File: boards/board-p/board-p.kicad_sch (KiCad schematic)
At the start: 0 parts

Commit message: feat: capture Board P schematic from the locked net table
Generated by scripts/schgen/gen_board_p.py: all 24 components placed
with global labels per pin, verified two ways with kicad-cli --
ERC passes with zero violations (including warnings) and the exported
netlist matches doc/architecture/board-p.mdx net-for-net (17 nets,
89 nodes, 6 intentional no-connects).

- symbols lib: all pins retyped passive (EasyEDA import had bogus
  Input types), Conn_1x04/Conn_1x08 pogo-pad symbols added
- footprints: PogoPad_1x04/1x08_P2.54mm hand-made pad arrays added
- C2/C35 use C14663 (0603, Basic) per the recommended Extended-fee
  swap in the docs; DNP parts (R17/R18, D6/D7) carry the dnp flag
- verify_netlist.py re-checks the schematic against the net table

Co-Authored-By: Claude <noreply@anthropic.com>
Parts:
- added C1: 10uF/50V, zudo-led-lamp:C1206, symbol zudo-led-lamp:CL31A106KBHNNNE
- added C2, C35: 100nF/50V, zudo-led-lamp:C0603, symbol zudo-led-lamp:CC0603KRX7R9BB104
- added C30, C34: 1uF/50V, zudo-led-lamp:C0603, symbol zudo-led-lamp:CL10A105KB8NNNC
- added D5: SMAJ20A, zudo-led-lamp:SMA_L4.2-W2.6-LS5.3-RD, symbol zudo-led-lamp:SMAJ20A_C571370
- added D6, D7: PESD24VS1UB, zudo-led-lamp:SOD-523_L1.2-W0.8-LS1.6-RD, symbol zudo-led-lamp:PESD24VS1UB,115
- added J1: TYPE-C-31-M-17, zudo-led-lamp:USB-C-SMD_10P-P1.00-L6.8-W8.9, symbol zudo-led-lamp:TYPE-C-31-M-17
- added J2: PogoPad_1x4_NVM_I2C, zudo-led-lamp:PogoPad_1x04_P2.54mm, symbol zudo-led-lamp:Conn_1x04
- added J3: PogoPad_1x8_Debug, zudo-led-lamp:PogoPad_1x08_P2.54mm, symbol zudo-led-lamp:Conn_1x08
- added JOUT1: B6B-XH-A(LF)(SN), zudo-led-lamp:CONN-TH_6P-P2.50_B6B-XH-A-LF-SN, symbol zudo-led-lamp:B6B-XH-A
- added Q1: AO3401A, zudo-led-lamp:SOT-23_L2.9-W1.3-P1.90-LS2.4-BR, symbol zudo-led-lamp:AO3401A_C347476
- added R11: 100k, zudo-led-lamp:R0603, symbol zudo-led-lamp:0603WAF1003T5E
- added R12: 56k, zudo-led-lamp:R0603, symbol zudo-led-lamp:0603WAF5602T5E
- added R13, R14: 470R, zudo-led-lamp:R0603, symbol zudo-led-lamp:0603WAF4700T5E
- added R15, R16: 4.7k, zudo-led-lamp:R0603, symbol zudo-led-lamp:0603WAF4701T5E
- added R17, R18: 5.1k, zudo-led-lamp:R0603, symbol zudo-led-lamp:0603WAF5101T5E
- added R19, R20: 0R, zudo-led-lamp:R0603, symbol zudo-led-lamp:0603WAF0000T5E
- added U1: STUSB4500QTR, zudo-led-lamp:QFN-24_L4.0-W4.0-P0.50-BL-EP2.8, symbol zudo-led-lamp:STUSB4500QTR
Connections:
- new net ATT: J3.6, JOUT1.3, U1.11 (ATTACH)
- new net CC1: D6.1 (C), J1.3 (A5), R17.1, R19.2, U1.2 (CC1)
- new net CC1DB: J3.1, R19.1, U1.1 (CC1DB)
- new net CC2: D7.1 (C), J1.4 (B5), R18.1, R20.2, U1.4 (CC2)
- new net CC2DB: J3.2, R20.1, U1.5 (CC2DB)
- new net DISCH: R13.2, U1.9 (DISCH)
- new net GND: C1.1, C2.1, C30.1, C34.2, C35.2, D5.2 (A), D6.2 (A), D7.2 (A), J1.0, J1.1 (B12), J1.6 (A12), J2.3, J3.5, JOUT1.5, JOUT1.6, R17.2, R18.2, U1.10 (GND), U1.12 (ADDR0), U1.13 (ADDR1), U1.22 (VSYS), U1.25 (EP), U1.6 (RESET)
- new net PDOK: J3.7, JOUT1.4, U1.20 (POWER_OK2)
- new net Q1_G: C35.1, Q1.1 (G), R11.1, R12.2
- new net SCL: J2.1, R15.1, U1.7 (SCL)
- new net SDA: J2.2, R16.1, U1.8 (SDA)
- new net VBEN: J3.8, R12.1, U1.16 (VBUS_EN_SNK)
- new net VBUS_IN: C1.2, C2.2, D5.1 (C), J1.2 (B9), J1.5 (A9), J3.4, Q1.2 (S), R11.2, R14.1, U1.24 (VDD)
- new net VBUS_OUT: JOUT1.1, JOUT1.2, Q1.3 (D), R13.1
- new net VBUS_VS_DISCH: R14.2, U1.18 (VBUS_VS_DISCH)
- new net VREG_1V2: C34.1, U1.21 (VREG_1V2)
- new net VREG_2V7: C30.2, J3.3, R15.2, R16.2, U1.23 (VREG_2V7)
- no-connect marks 0 -> 6

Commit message: feat: capture Board L schematic; refactor generator into spec-driven core
Board L: all 68 components (driver, LED array 8x3, logic rail, MCU,
encoder, debug pads) captured from the locked net table in
doc/architecture/board-l.mdx. ERC passes with zero violations and the
exported netlist matches the spec: 45 nets, 178 nodes, 11 intentional
no-connects. Board P regenerated through the same pipeline, still
ERC-clean and netlist-verified.

- scripts/schgen split into schgen_core.py + board_p_spec.py /
  board_l_spec.py + generic gen_schematic.py / verify_netlist.py,
  so the net table lives in exactly one place per board
- symbols lib normalized via kicad-cli sym upgrade (two inductor
  symbols were in legacy KiCad 6 format and tripped
  lib_symbol_mismatch ERC warnings); Conn_1x03 symbol added
- PogoPad_1x03_P2.54mm hand-made UART pad footprint added
- J3 (SWD header) and J4 (UART pads) carry the DNP flag: footprint
  only, excluded from the assembly BOM per the bring-up plan
- LED polarity taken from the symbol drawing: pin 1 = cathode,
  pin 2 = anode; EC11 push-button terminals D/E left no-connect

Co-Authored-By: Claude <noreply@anthropic.com>
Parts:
- D6, D7, R17, R18: DNP DNP -> (none)
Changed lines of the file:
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@@
 			)
+		)
+		(pin "0"
+		)
+		(pin "0"
+		)
+		(pin "0"
+		)
+		(pin "0"
 		)
 		(pin "1"
@@
 		(pin "6"
 		)
-		(pin "0"
-		)
-		(pin "0"
-		)
-		(pin "0"
-		)
-		(pin "0"
-		)
-		(instances
-			(project "board-p"
-				(path "/b2dc3f53-49f5-4fb9-8f78-98d4bdbdbabb"
+		(instances
+			(project "board-p"
+				(path "/2f50887c-fd80-4f71-a2f8-d8c1a887c3bf"
 					(reference "J1")
 					(unit 1)
@@
 		(instances
 			(project "board-p"
-				(path "/b2dc3f53-49f5-4fb9-8f78-98d4bdbdbabb"
+				(path "/2f50887c-fd80-4f71-a2f8-d8c1a887c3bf"
 					(reference "U1")
 					(unit 1)
@@
 			)
 		)
+		(pin "1"
+		)
+		(pin "2"
+		)
 		(pin "3"
 		)
-		(pin "1"
-		)
-		(pin "2"
-		)
-		(instances
-			(project "board-p"
-				(path "/b2dc3f53-49f5-4fb9-8f78-98d4bdbdbabb"
+		(instances
+			(project "board-p"
+				(path "/2f50887c-fd80-4f71-a2f8-d8c1a887c3bf"
 					(reference "Q1")
 					(unit 1)
@@
 			)
 		)
-		(pin "2"
-		)
-		(pin "1"
-		)
-		(instances
-			(project "board-p"
-				(path "/b2dc3f53-49f5-4fb9-8f78-98d4bdbdbabb"
+		(pin "1"
+		)
+		(pin "2"
+		)
+		(instances
+			(project "board-p"
+				(path "/2f50887c-fd80-4f71-a2f8-d8c1a887c3bf"
 					(reference "D5")
 					(unit 1)
@@
 			)
 		)
-		(property "DNP" "DNP"
-			(at 228.6 175.26 0)
-			(effects
-				(font (size 1.27 1.27))
-				(hide yes)
-			)
-		)
-		(pin "2"
-		)
-		(pin "1"
-		)
-		(instances
-			(project "board-p"
-				(path "/b2dc3f53-49f5-4fb9-8f78-98d4bdbdbabb"
+		(pin "1"
+		)
+		(pin "2"
+		)
+		(instances
+			(project "board-p"
+				(path "/2f50887c-fd80-4f71-a2f8-d8c1a887c3bf"
 					(reference "D6")
 					(unit 1)
@@
 			)
 		)
-		(property "DNP" "DNP"
-			(at 190.5 226.06 0)
-			(effects
-				(font (size 1.27 1.27))
-				(hide yes)
-			)
-		)
-		(pin "2"
-		)
-		(pin "1"
-		)
-		(instances
-			(project "board-p"
-				(path "/b2dc3f53-49f5-4fb9-8f78-98d4bdbdbabb"
+		(pin "1"
+		)
+		(pin "2"
+		)
+		(instances
+			(project "board-p"
+				(path "/2f50887c-fd80-4f71-a2f8-d8c1a887c3bf"
 					(reference "D7")
 					(unit 1)
@@
 		(instances
 			(project "board-p"
-				(path "/b2dc3f53-49f5-4fb9-8f78-98d4bdbdbabb"
+				(path "/2f50887c-fd80-4f71-a2f8-d8c1a887c3bf"
 					(reference "C1")
 					(unit 1)
@@
 		(instances
 			(project "board-p"
-				(path "/b2dc3f53-49f5-4fb9-8f78-98d4bdbdbabb"
+				(path "/2f50887c-fd80-4f71-a2f8-d8c1a887c3bf"
 					(reference "C2")
 					(unit 1)
@@
 			)
 		)
-		(pin "2"
-		)
-		(pin "1"
-		)
-		(instances
-			(project "board-p"
-				(path "/b2dc3f53-49f5-4fb9-8f78-98d4bdbdbabb"
+		(pin "1"
+		)
+		(pin "2"
+		)
+		(instances
+			(project "board-p"
+				(path "/2f50887c-fd80-4f71-a2f8-d8c1a887c3bf"
 					(reference "C30")
 					(unit 1)
@@
 			)
 		)
-		(pin "2"
-		)
-		(pin "1"
-		)
-		(instances
-			(project "board-p"
-				(path "/b2dc3f53-49f5-4fb9-8f78-98d4bdbdbabb"
+		(pin "1"
+		)
+		(pin "2"
+		)
+		(instances
+			(project "board-p"
+				(path "/2f50887c-fd80-4f71-a2f8-d8c1a887c3bf"
 					(reference "C34")
 					(unit 1)
@@
 		(instances
 			(project "board-p"
-				(path "/b2dc3f53-49f5-4fb9-8f78-98d4bdbdbabb"
+				(path "/2f50887c-fd80-4f71-a2f8-d8c1a887c3bf"
 					(reference "C35")
 					(unit 1)
@@
 			)
 		)
-		(pin "2"
-		)
-		(pin "1"
-		)
-		(instances
-			(project "board-p"
-				(path "/b2dc3f53-49f5-4fb9-8f78-98d4bdbdbabb"
+		(pin "1"
+		)
+		(pin "2"
+		)
+		(instances
+			(project "board-p"
+				(path "/2f50887c-fd80-4f71-a2f8-d8c1a887c3bf"
 					(reference "R11")
 					(unit 1)
@@
 			)
 		)
-		(pin "2"
-		)
-		(pin "1"
-		)
-		(instances
-			(project "board-p"
-				(path "/b2dc3f53-49f5-4fb9-8f78-98d4bdbdbabb"
+		(pin "1"
+		)
+		(pin "2"
+		)
+		(instances
+			(project "board-p"
+				(path "/2f50887c-fd80-4f71-a2f8-d8c1a887c3bf"
 					(reference "R12")
 					(unit 1)
@@
 			)
 		)
-		(pin "2"
-		)
-		(pin "1"
-		)
-		(instances
-			(project "board-p"
-				(path "/b2dc3f53-49f5-4fb9-8f78-98d4bdbdbabb"
+		(pin "1"
+		)
+		(pin "2"
+		)
+		(instances
+			(project "board-p"
+				(path "/2f50887c-fd80-4f71-a2f8-d8c1a887c3bf"
 					(reference "R13")
 					(unit 1)
@@
 			)
 		)
-		(pin "2"
-		)
-		(pin "1"
-		)
-		(instances
-			(project "board-p"
-				(path "/b2dc3f53-49f5-4fb9-8f78-98d4bdbdbabb"
+		(pin "1"
+		)
+		(pin "2"
+		)
+		(instances
+			(project "board-p"
+				(path "/2f50887c-fd80-4f71-a2f8-d8c1a887c3bf"
 					(reference "R14")
 					(unit 1)
@@
 			)
 		)
-		(pin "2"
-		)
-		(pin "1"
-		)
-		(instances
-			(project "board-p"
-				(path "/b2dc3f53-49f5-4fb9-8f78-98d4bdbdbabb"
+		(pin "1"
+		)
+		(pin "2"
+		)
+		(instances
+			(project "board-p"
+				(path "/2f50887c-fd80-4f71-a2f8-d8c1a887c3bf"
 					(reference "R15")
 					(unit 1)
@@
 			)
 		)
-		(pin "2"
-		)
-		(pin "1"
-		)
-		(instances
-			(project "board-p"
-				(path "/b2dc3f53-49f5-4fb9-8f78-98d4bdbdbabb"
+		(pin "1"
+		)
+		(pin "2"
+		)
+		(instances
+			(project "board-p"
+				(path "/2f50887c-fd80-4f71-a2f8-d8c1a887c3bf"
 					(reference "R16")
 					(unit 1)
@@
 			)
 		)
-		(property "DNP" "DNP"
-			(at 38.1 226.06 0)
-			(effects
-				(font (size 1.27 1.27))
-				(hide yes)
-			)
-		)
-		(pin "2"
-		)
-		(pin "1"
-		)
-		(instances
-			(project "board-p"
-				(path "/b2dc3f53-49f5-4fb9-8f78-98d4bdbdbabb"
+		(pin "1"
+		)
+		(pin "2"
+		)
+		(instances
+			(project "board-p"
+				(path "/2f50887c-fd80-4f71-a2f8-d8c1a887c3bf"
 					(reference "R17")
 					(unit 1)
@@
 			)
 		)
-		(property "DNP" "DNP"
-			(at 76.2 226.06 0)
-			(effects
-				(font (size 1.27 1.27))
-				(hide yes)
-			)
-		)
-		(pin "2"
-		)
-		(pin "1"
-		)
-		(instances
-			(project "board-p"
-				(path "/b2dc3f53-49f5-4fb9-8f78-98d4bdbdbabb"
+		(pin "1"
+		)
+		(pin "2"
+		)
+		(instances
+			(project "board-p"
+				(path "/2f50887c-fd80-4f71-a2f8-d8c1a887c3bf"
 					(reference "R18")
 					(unit 1)
@@
 			)
 		)
-		(pin "2"
-		)
-		(pin "1"
-		)
-		(instances
-			(project "board-p"
-				(path "/b2dc3f53-49f5-4fb9-8f78-98d4bdbdbabb"
+		(pin "1"
+		)
+		(pin "2"
+		)
+		(instances
+			(project "board-p"
+				(path "/2f50887c-fd80-4f71-a2f8-d8c1a887c3bf"
 					(reference "R19")
 					(unit 1)
@@
 			)
 		)
-		(pin "2"
-		)
-		(pin "1"
-		)
-		(instances
-			(project "board-p"
-				(path "/b2dc3f53-49f5-4fb9-8f78-98d4bdbdbabb"
+		(pin "1"
+		)
+		(pin "2"
+		)
+		(instances
+			(project "board-p"
+				(path "/2f50887c-fd80-4f71-a2f8-d8c1a887c3bf"
 					(reference "R20")
 					(unit 1)
@@
 		(instances
 			(project "board-p"
-				(path "/b2dc3f53-49f5-4fb9-8f78-98d4bdbdbabb"
+				(path "/2f50887c-fd80-4f71-a2f8-d8c1a887c3bf"
 					(reference "JOUT1")
 					(unit 1)
@@
 		(instances
 			(project "board-p"
-				(path "/b2dc3f53-49f5-4fb9-8f78-98d4bdbdbabb"
+				(path "/2f50887c-fd80-4f71-a2f8-d8c1a887c3bf"
 					(reference "J2")
 					(unit 1)
@@
 		(instances
 			(project "board-p"
-				(path "/b2dc3f53-49f5-4fb9-8f78-98d4bdbdbabb"
+				(path "/2f50887c-fd80-4f71-a2f8-d8c1a887c3bf"
 					(reference "J3")
 					(unit 1)

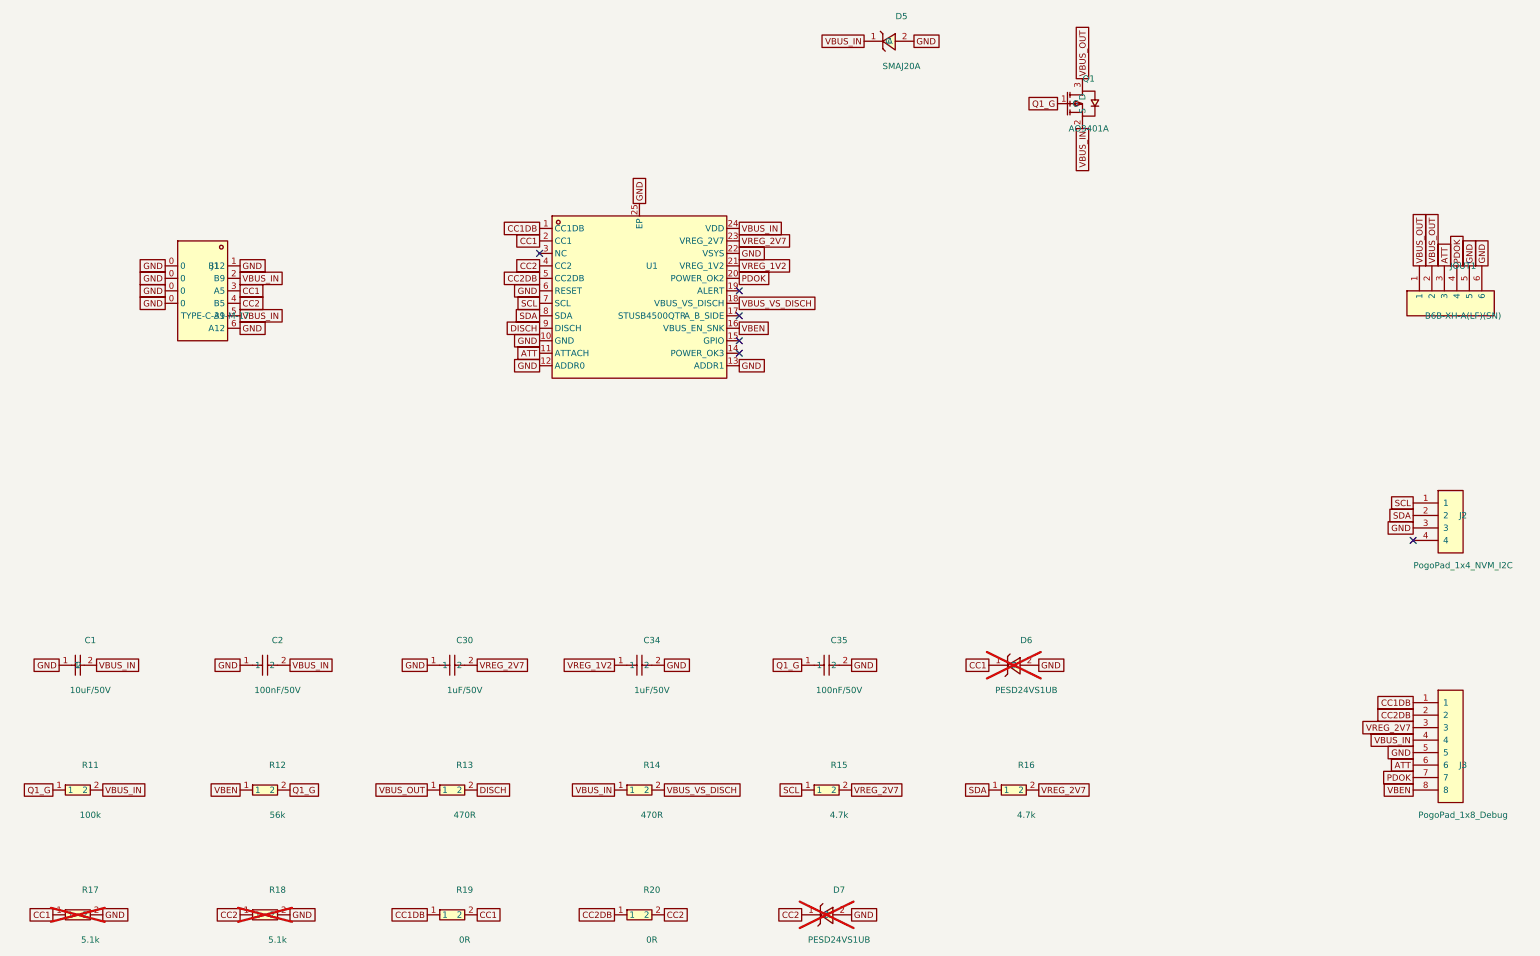
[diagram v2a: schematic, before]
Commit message: fix: schematic readability — labels outside bodies, Board L on A2
- reference/value text now placed from the symbol's pin extents
  (above/below the body) instead of a fixed offset that landed inside
  large IC bodies; per-ref overrides for Q1 and SW1 where vertical
  net labels occupy the default spots
- Board L moved to A2: the 68-part grid collided with the A3 title
  block and bottom border
- connectivity unchanged: both boards still ERC-clean and
  netlist-verified against their specs

Co-Authored-By: Claude <noreply@anthropic.com>
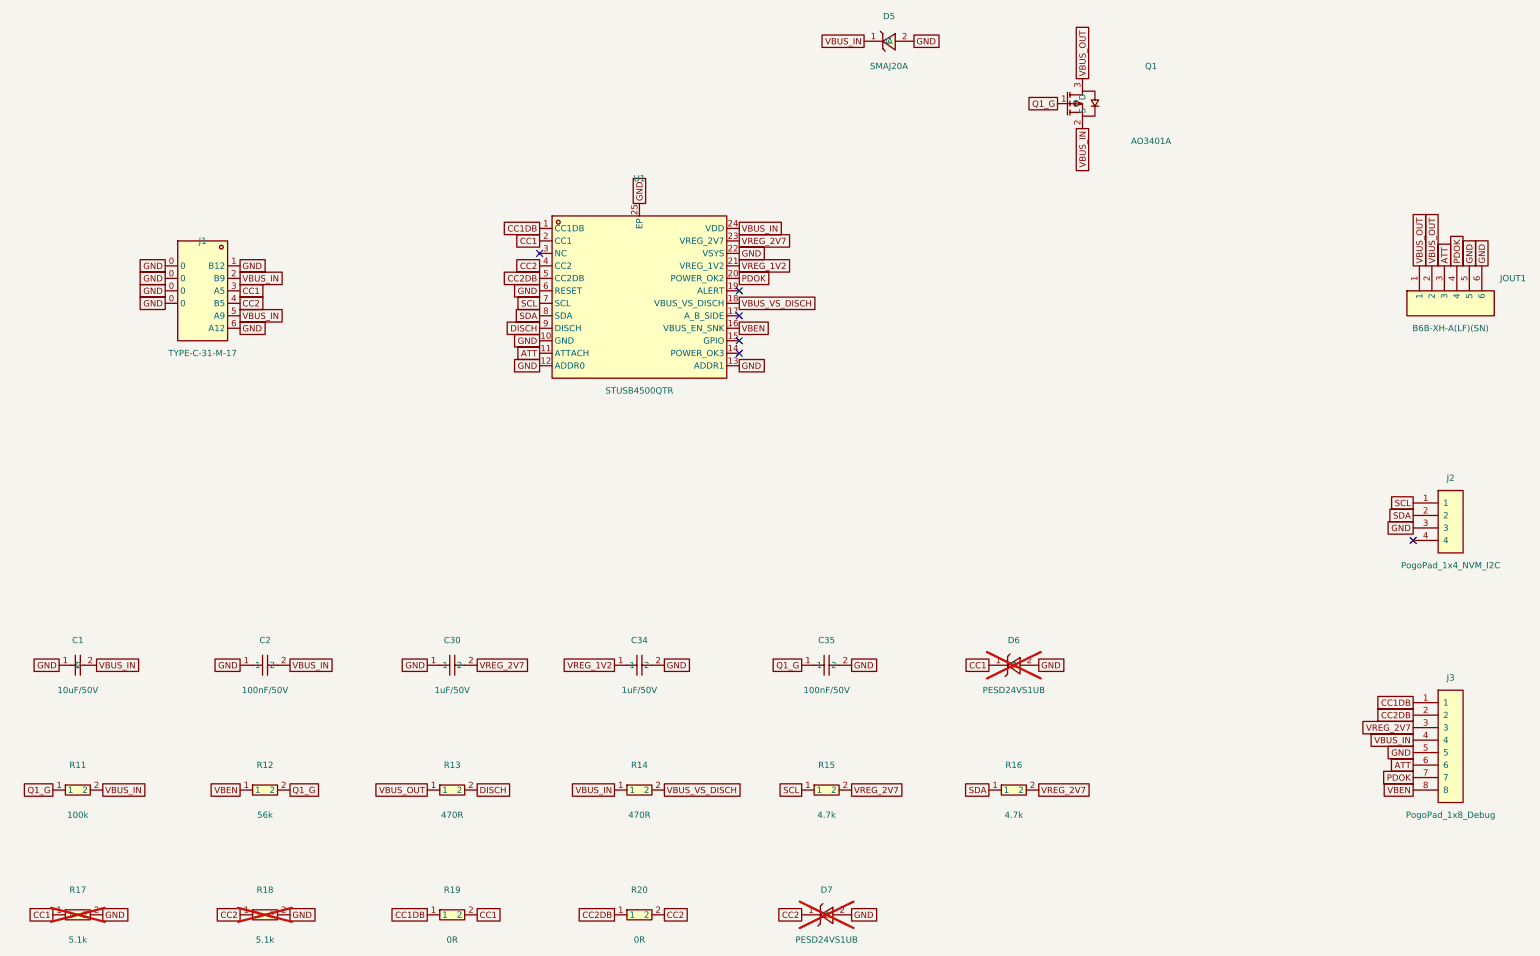
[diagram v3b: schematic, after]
